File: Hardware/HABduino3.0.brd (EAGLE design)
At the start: 68.5 x 53.4 mm, 43 parts, among them IC2 TPS61201, U1 ARDUINO_SHIELDNO_SILK, U2 LM3480IM3-3.3, U3 TXS0102DCTT

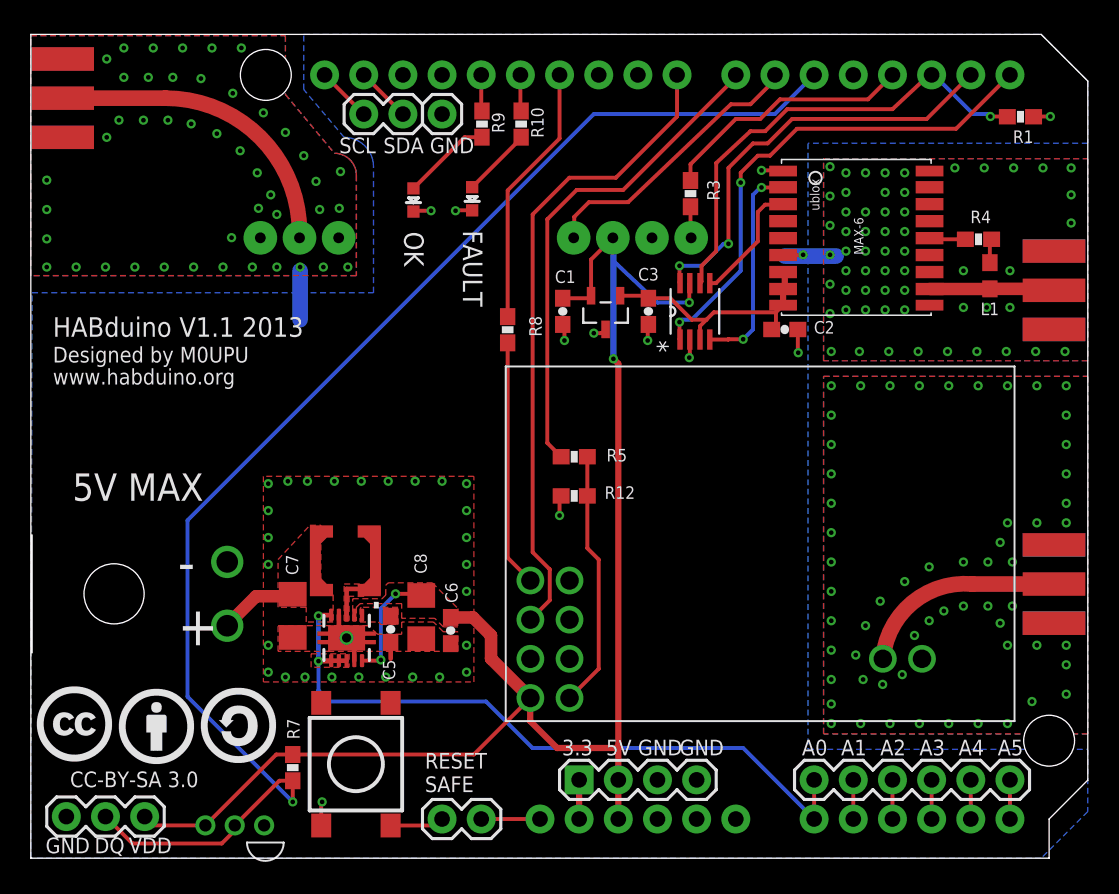
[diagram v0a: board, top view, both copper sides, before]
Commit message: New hardware version 3.0
Removed LMT2 and replaced with MTX2 transmitter.
Removed TO92 DS18B20 and replaced with SMD version.
Removed Reset Protect + Reset switch
Switch power supply +/- round to match the Pi In The Sky.
Minor Silk Screen amendments.
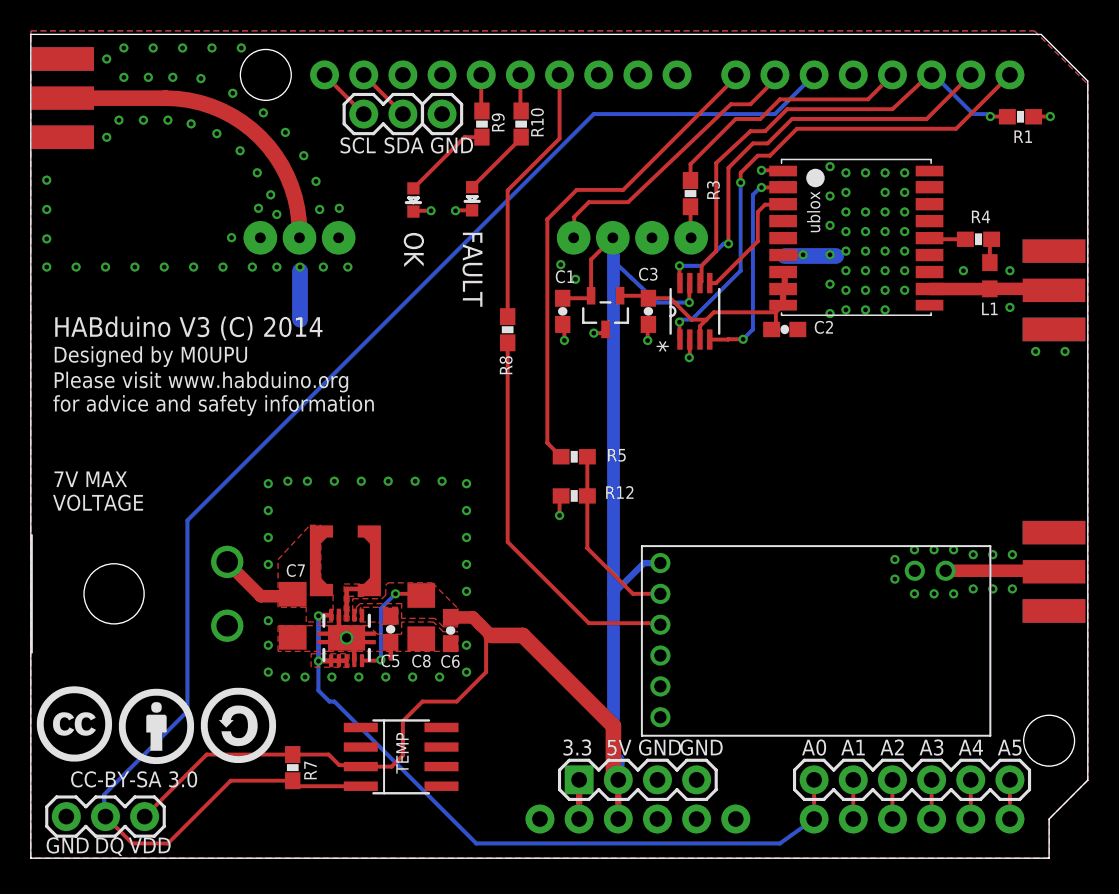
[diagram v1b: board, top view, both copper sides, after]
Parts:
- removed RESET_LOCKOUT: (no value), SparkFun:1X02
- removed S1: RESET, SparkFun:TACTILE_SWITCH_TALL
- removed TEMPINT: DS1821, ava:DS1820
- removed U$2: RADIOMETRIX_LMT2, ava:RADIOMETRIX-LMT2
- added TEMP: DS1821, ava:DS18B20_SOIC
- added U$4: RADIOMETRIX-MTX2, ava:RADIOMETRIX-MTX2
- U$1: value UBLOX_MAX-6 -> UBLOX_MAX; device ava:UBLOX_MAX-6 -> ava:UBLOX_MAX
- moved J$1 0.79 mm to (66.4, 18.6)
- renumbered U$10 to LPS4018
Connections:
- net 11/LMT2_TXD renamed 11/MTX2_TXD
- net 7/LMT2_P0 renamed 7/MTX2_EN
- removed net 10/: U1.D10
- removed net 8/LMT2_N_TXD: U$2.N_TXE, U1.D8
- removed net 9/NC: U1.D9
- removed net LMT2_P0: R12.2, R5.1, U$2.P0/PGM
- removed net N$6: RESET_LOCKOUT.1, S1.B2
- removed net _LMT2TXD: R8.2, U$2.TXD
- new net MTX2EN: R12.2, R5.1, U$4.EN
- net 5/TEMPSENSORS: now also TEMP.DQ; no longer TEMPINT.DQ
- net A0/VBATT: now also U$9.P$1; no longer U$9.P$2
- net GND: now also TEMP.GND, U$4.GND, U$4.RFGND, U$9.P$2; no longer S1.A2, TEMPINT.GND, U$2.GND, U$2.RFGND, U$9.P$1
- net N$3: now also U$4.RF; no longer U$2.RF
- net N$7: now also R8.2, U$4.TXD; no longer RESET_LOCKOUT.2, U1.RES
- net V5V: now also TEMP.VCC, U$4.VCC; no longer TEMPINT.VDD, U$2.VCC
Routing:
- net 8/LMT2_N_TXD: track 42.0 -> 0.00 mm
- net N$7: track 3.81 -> 25.0 mm
- net LMT2_P0: track 16.7 -> 0.00 mm
- net _LMT2TXD: track 16.0 -> 0.00 mm
- net MTX2EN: track 0.00 -> 11.9 mm
- net V5V: track 104.8 -> 112.2 mm, vias 4 -> 3
- net N$3: track 12.9 -> 7.09 mm
- net N$6: track 3.51 -> 0.00 mm
- net 5/TEMPSENSORS: track 89.9 -> 93.2 mm, vias 1 -> 0
- net GND: track 24.9 -> 21.8 mm, vias 202 -> 140
- net A0/VBATT: track 53.5 -> 54.8 mm
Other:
- board text added: "(C) HABduino Project 2014 http://habduino.org Please visit website for assitance with legislation and safety advice. In most countries you will need to seek permission to launch a meteorological balloon. http://ukhas.org.uk http://spacenear.us/tracker"
- board text added: "7V MAX VOLTAGE"
- board text added: "HABduino V3 (C) 2014"
- board text added: "Please visit www.habduino.org for advice and safety information"
- board text removed: "(C) HABduino Project 2013 http://habduino.org Please visit website for assitance with legislation and safety advice. In most countries you will need to seek permission to launch a meteorological balloon. http://ukhas.org.uk http://spacenear.us/tracker"
- board text removed: "+"
- board text removed: "-"
- board text removed: "."
- board text removed: "5V MAX"
- board text removed: "HABduino V1.1 2013"
- board text removed: "RESET SAFE"
- board text removed: "www.habduino.org"
